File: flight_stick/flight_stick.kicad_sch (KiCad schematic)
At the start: 59 parts, among them J1 Load Cell 1, J10 USB_C_Receptacle_USB2.0, J11 Conn_01x05_Pin, J3 Load Cell 2, J5 Load Cell 3, J7 Conn_01x04_Male, J8 Conn_01x05_Pin, J9 Conn_ST_STDC14, Q4 2N7002, Q5 2N7002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

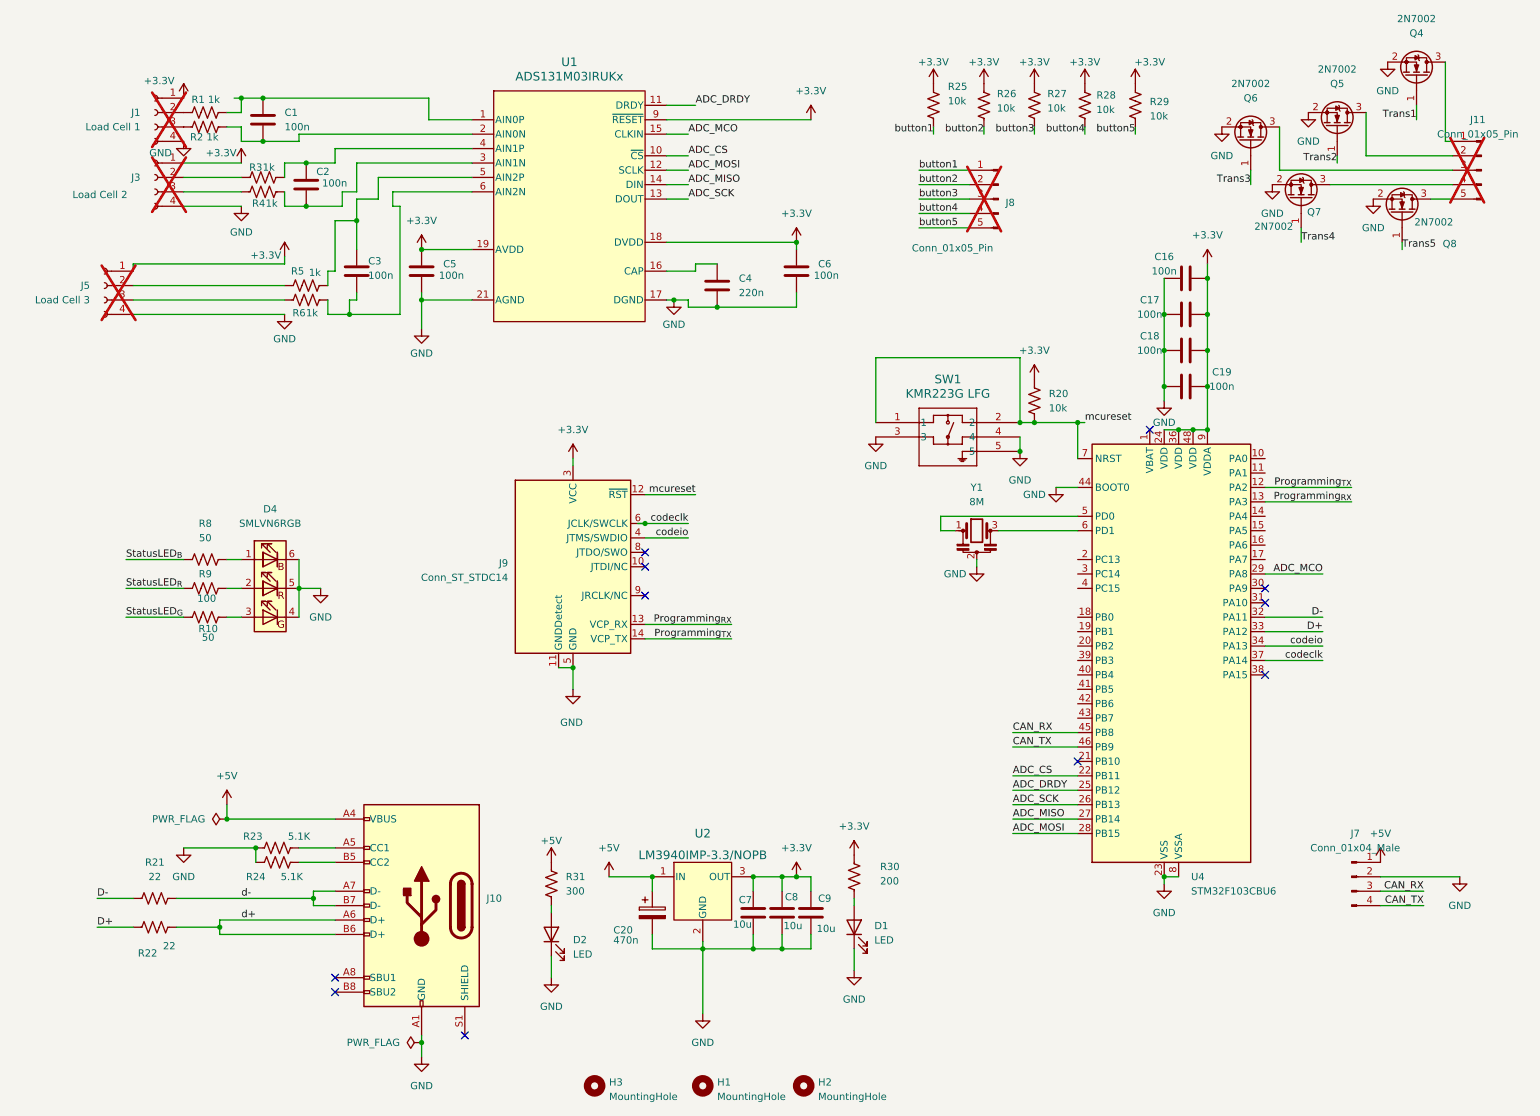
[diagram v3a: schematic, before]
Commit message: Moving REV5 to new repo
moving to hpvdt/falcon_flight_stick
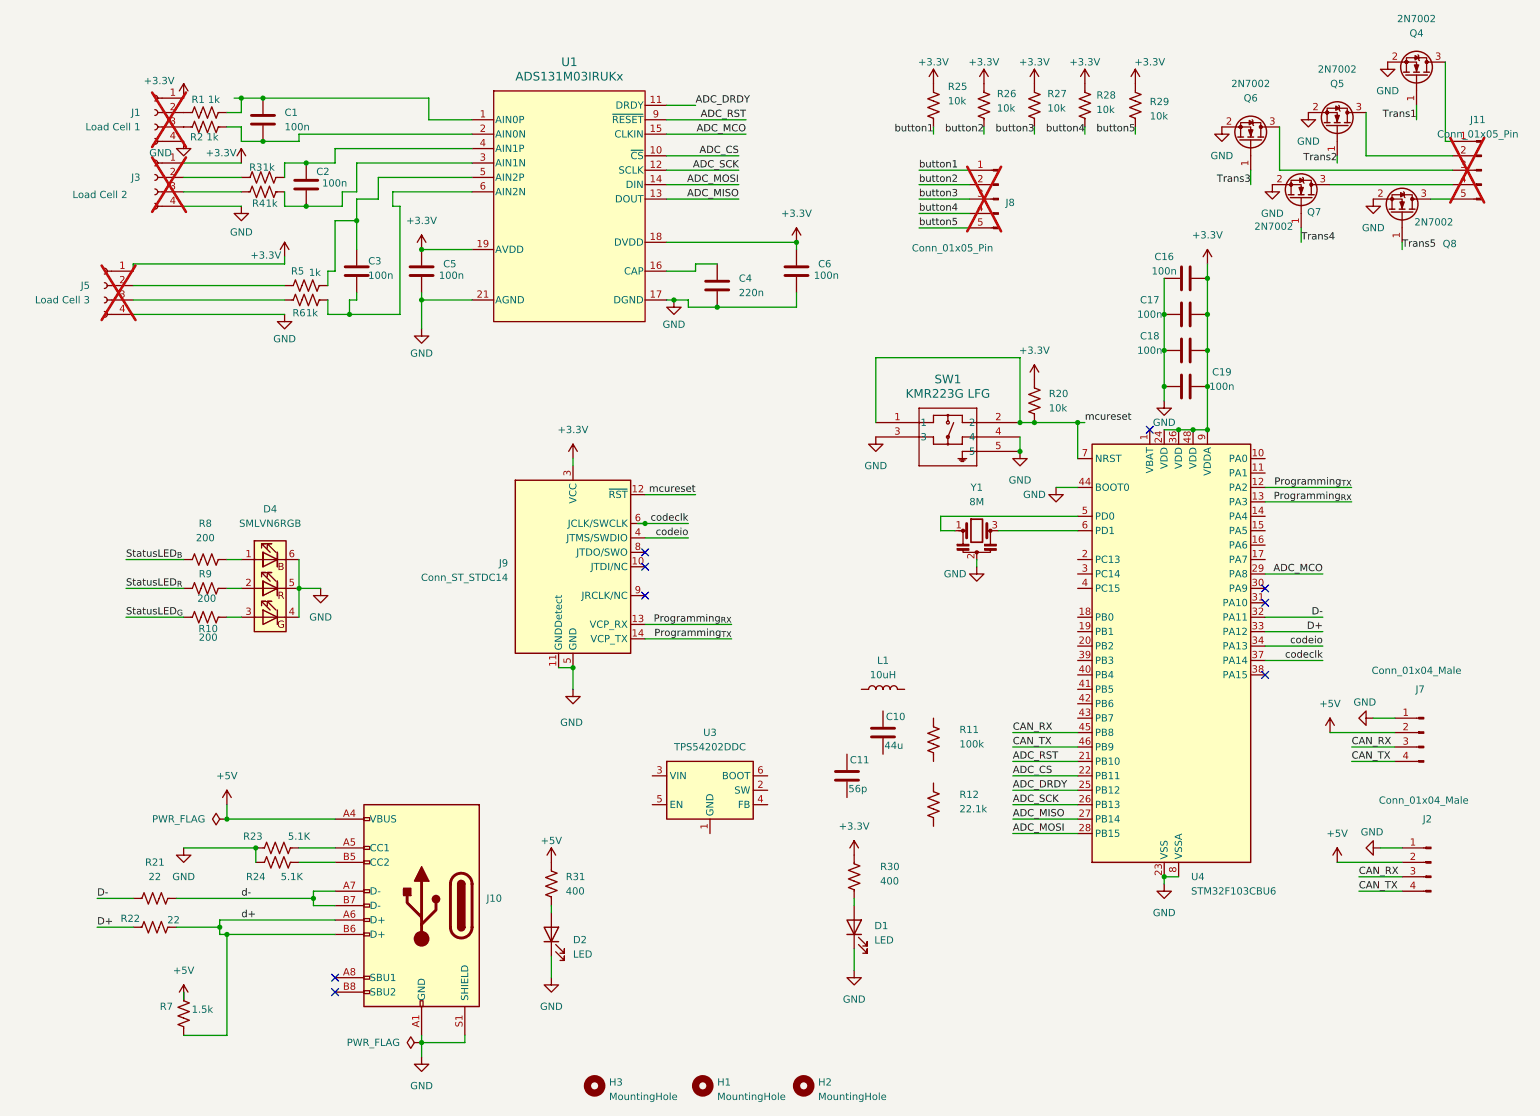
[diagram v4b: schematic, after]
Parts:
- removed C20: 470n, Capacitor_SMD:C_0603_1608Metric, symbol Device:C_Polarized
- removed C7, C8, C9: 10u, Capacitor_SMD:C_0603_1608Metric, symbol Device:C
- removed U2: LM3940IMP-3.3/NOPB, flight_stick_footprints:MP04A, symbol flight_stick:LM3940IMP-3.3_NOPB
- added C10: 44u, Capacitor_SMD:C_0603_1608Metric, symbol Device:C
- added C11: 56p, Capacitor_SMD:C_0603_1608Metric, symbol Device:C
- added J2: Conn_01x04_Male, Connector_JST:JST_XH_B4B-XH-A_1x04_P2.50mm_Vertical, symbol Connector:Conn_01x04_Pin
- added L1: 10uH, symbol Device:L
- added R11: 100k, Resistor_SMD:R_0603_1608Metric, symbol Device:R_US
- added R12: 22.1k, Resistor_SMD:R_0603_1608Metric, symbol Device:R_US
- added R7: 1.5k, Resistor_SMD:R_0603_1608Metric, symbol Device:R_US
- added U3: TPS54202DDC, Package_TO_SOT_SMD:SOT-23-6, symbol Regulator_Switching:TPS54202DDC
- R10, R8: value 50 -> 200
- R30: value 200 -> 400
- R31: value 300 -> 400
- R9: value 100 -> 200
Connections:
- net +3.3V: no longer U1.9 (~{RESET})
- net +5V: now also J7.2 (Pin_2), J2.2 (Pin_2), R7.2; no longer J7.1 (Pin_1)
- net ADC_MISO: now also U1.13 (DOUT); no longer U1.14 (DIN)
- net ADC_MOSI: now also U1.14 (DIN); no longer U1.12 (SCLK)
- net ADC_SCK: now also U1.12 (SCLK); no longer U1.13 (DOUT)
- net AGND: now also J10.S1 (SHIELD), J7.1 (Pin_1), J2.1 (Pin_1); no longer J7.2 (Pin_2)
- net CAN_RX: now also J2.3 (Pin_3)
- net CAN_TX: now also J2.4 (Pin_4)
- net d+: now also R7.1
- net ADC_RST: now reaches U4.21 (PB10)
- net ADC_RST: now also U1.9 (~{RESET})
- no-connect marks 11 -> 9
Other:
- moved on the sheet: J7
